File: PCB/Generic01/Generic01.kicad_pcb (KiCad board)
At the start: 2 copper layers, 13.2 x 18 mm, 3 parts, among them J1 Header, U1 ESP32-PICO-MINI-02

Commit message: Production files
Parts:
- moved Logo1 5.36 mm to (145.3, 118.1), turned to -90 degrees
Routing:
- net VCC: track 23.7 -> 21.7 mm
- net EN: track 14.8 -> 16.5 mm
- net RX: track 9.35 -> 9.96 mm
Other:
- board text added: "${CURRENT_DATE}"
- board text added: "3V3"
- board text added: "EN"
- board text added: "ESP32-01"
- board text added: "GND"
- board text added: "IO0"
- board text added: "IO2"
- board text added: "IO4"
- board text added: "RX"
- board text added: "TX"

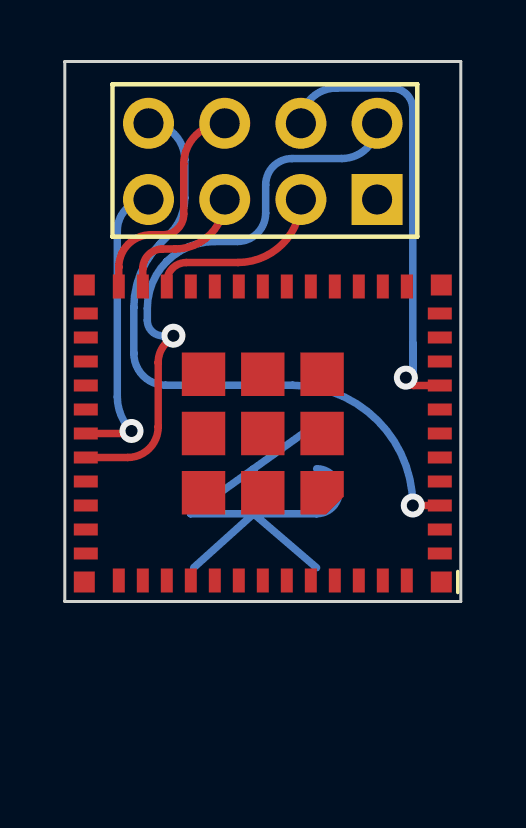
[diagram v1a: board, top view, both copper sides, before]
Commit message: Move RST
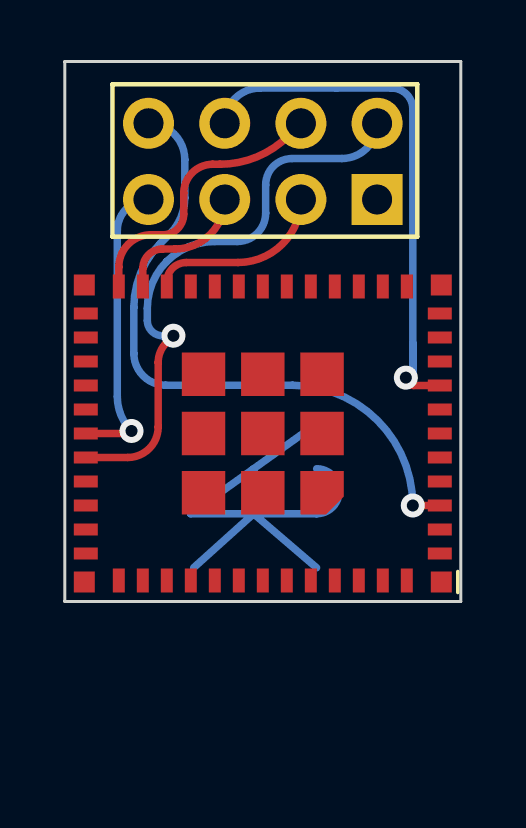
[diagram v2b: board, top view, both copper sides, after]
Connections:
- J1 pad 4: EN -> GPIO4
- J1 pad 6: GPIO4 -> EN
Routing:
- net EN: track 16.5 -> 19.1 mm
- net GPIO4: track 7.50 -> 9.27 mm
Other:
- board text added: "RST"
- board text removed: "EN"

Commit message: Tidy RST as EN
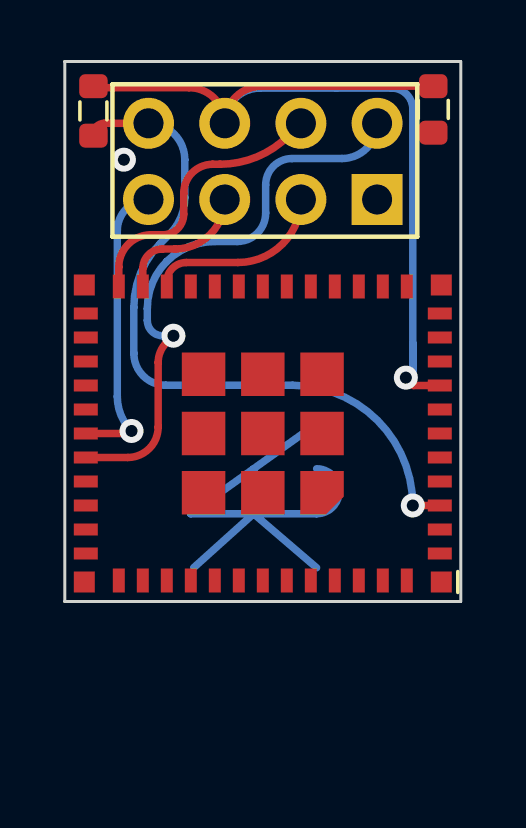
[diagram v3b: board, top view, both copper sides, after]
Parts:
- added C1: 1uF, RevK:C_0603, F.Cu at (151.3, 104.6)
- added R1: 12k, RevK:R_0603, F.Cu at (140.0, 104.6)
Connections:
- net EN renamed RST
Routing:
- net RST: track 19.1 -> 31.7 mm
- net VCC: track 21.7 -> 23.7 mm
- net GND: vias 0 -> 1
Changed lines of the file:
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@@
   (net 20 "unconnected-(U1-IO13-Pad20)")
   (net 21 "unconnected-(U1-IO15-Pad21)")
-  (net 22 "EN")
+  (net 22 "RST")
   (net 23 "unconnected-(U1-NC-Pad25)")
   (net 24 "unconnected-(U1-IO20-Pad26)")
@@
       (net 10 "unconnected-(U1-I39-Pad7)") (pinfunction "I39") (pintype "input+no_connect"))
     (pad "8" smd rect (at -5.9 1.6 180) (size 0.8 0.4) (layers "F.Cu" "F.Paste" "F.Mask")
-      (net 22 "EN") (pinfunction "EN") (pintype "input"))
+      (net 22 "RST") (pinfunction "EN") (pintype "input"))
     (pad "9" smd rect (at -5.9 2.4 180) (size 0.8 0.4) (layers "F.Cu" "F.Paste" "F.Mask")
       (net 11 "unconnected-(U1-I34-Pad9)") (pinfunction "I34") (pintype "input+no_connect"))
@@
     )
   )
+  (footprint "RevK:R_0603" (layer "F.Cu")
+    (at 139.954 104.648 90)
+    (descr "Capacitor SMD 0603 (1608 Metric), square (rectangular) end terminal, IPC_7351 nominal, (Body size source: IPC-SM-782 page 76, https://www.pcb-3d.com/wordpress/wp-content/uploads/ipc-sm-782a_amendment_1_and_2.pdf), generated with kicad-footprint-generator")
+    (tags "capacitor")
+    (property "Sheetfile" "Generic01.kicad_sch")
+    (property "Sheetname" "")
+    (property "ki_description" "Resistor")
+    (property "ki_keywords" "R res resistor")
+    (attr smd)
+    (fp_text reference "R1" (at -1.6 0 180) (layer "F.SilkS") hide
+        (effects (font (size 0.5 0.5) (thickness 0.08)))
+    )
+    (fp_text value "12k" (at 0 0 90) (layer "F.Fab")
+        (effects (font (size 0.4 0.4) (thickness 0.08)))
+    )
+    (fp_text user "${REFERENCE}" (at 0 -0.8 90) (layer "F.Fab")
+        (effects (font (size 0.4 0.4) (thickness 0.06)))
+    )
+    (fp_line (start -0.3 -0.45) (end 0.3 -0.45)
+      (stroke (width 0.12) (type solid)) (layer "F.SilkS"))
+    (fp_line (start -0.3 0.45) (end 0.3 0.45)
+      (stroke (width 0.12) (type solid)) (layer "F.SilkS"))
+    (fp_line (start -0.8 -0.4) (end 0.8 -0.4)
+      (stroke (width 0.05) (type solid)) (layer "F.CrtYd"))
+    (fp_line (start -0.8 0.4) (end -0.8 -0.4)
+      (stroke (width 0.05) (type solid)) (layer "F.CrtYd"))
+    (fp_line (start 0.8 -0.4) (end 0.8 0.4)
+      (stroke (width 0.05) (type solid)) (layer "F.CrtYd"))
+    (fp_line (start 0.8 0.4) (end -0.8 0.4)
+      (stroke (width 0.05) (type solid)) (layer "F.CrtYd"))
+    (fp_line (start -0.8 -0.4) (end 0.8 -0.4)
+      (stroke (width 0.1) (type solid)) (layer "F.Fab"))
+    (fp_line (start -0.8 0.4) (end -0.8 -0.4)
+      (stroke (width 0.1) (type solid)) (layer "F.Fab"))
+    (fp_line (start 0.8 -0.4) (end 0.8 0.4)
+      (stroke (width 0.1) (type solid)) (layer "F.Fab"))
+    (fp_line (start 0.8 0.4) (end -0.8 0.4)
+      (stroke (width 0.1) (type solid)) (layer "F.Fab"))
+    (pad "1" smd roundrect (at -0.825 0 90) (size 0.8 0.95) (layers "F.Cu" "F.Paste" "F.Mask") (roundrect_rratio 0.25)
+      (net 6 "VCC") (pintype "passive"))
+    (pad "2" smd roundrect (at 0.825 0 90) (size 0.8 0.95) (layers "F.Cu" "F.Paste" "F.Mask") (roundrect_rratio 0.25)
+      (net 22 "RST") (pintype "passive"))
+    (model "${KICAD6_3DMODEL_DIR}/Resistor_SMD.3dshapes/R_0603_1608Metric.step"
+      (offset (xyz 0 0 0))
+      (scale (xyz 1 1 1))
+      (rotate (xyz 0 0 0))
+    )
+  )
+  (footprint "RevK:C_0603" (layer "F.Cu")
+    (at 151.2824 104.5972 -90)
+    (descr "Capacitor SMD 0603 (1608 Metric), square (rectangular) end terminal, IPC_7351 nominal, (Body size source: IPC-SM-782 page 76, https://www.pcb-3d.com/wordpress/wp-content/uploads/ipc-sm-782a_amendment_1_and_2.pdf), generated with kicad-footprint-generator")
+    (tags "capacitor")
+    (property "Sheetfile" "Generic01.kicad_sch")
+    (property "Sheetname" "")
+    (property "ki_description" "Unpolarized capacitor")
+    (property "ki_keywords" "cap capacitor")
+    (attr smd)
+    (fp_text reference "C1" (at -1.6 0) (layer "F.SilkS") hide
+        (effects (font (size 0.5 0.5) (thickness 0.08)))
+    )
+    (fp_text value "1uF" (at 0 0 90) (layer "F.Fab")
+        (effects (font (size 0.4 0.4) (thickness 0.08)))
+    )
+    (fp_text user "${REFERENCE}" (at 0 -0.8 90) (layer "F.Fab")
+        (effects (font (size 0.4 0.4) (thickness 0.06)))
+    )
+    (fp_line (start -0.3 -0.5) (end 0.3 -0.5)
+      (stroke (width 0.12) (type solid)) (layer "F.SilkS"))
+    (fp_line (start -0.3 0.5) (end 0.3 0.5)
+      (stroke (width 0.12) (type solid)) (layer "F.SilkS"))
+    (fp_line (start -0.8 -0.4) (end 0.8 -0.4)
+      (stroke (width 0.05) (type solid)) (layer "F.CrtYd"))
+    (fp_line (start -0.8 0.4) (end -0.8 -0.4)
+      (stroke (width 0.05) (type solid)) (layer "F.CrtYd"))
+    (fp_line (start 0.8 -0.4) (end 0.8 0.4)
+      (stroke (width 0.05) (type solid)) (layer "F.CrtYd"))
+    (fp_line (start 0.8 0.4) (end -0.8 0.4)
+      (stroke (width 0.05) (type solid)) (layer "F.CrtYd"))
+    (fp_line (start -0.8 -0.4) (end 0.8 -0.4)
+      (stroke (width 0.1) (type solid)) (layer "F.Fab"))
+    (fp_line (start -0.8 0.4) (end -0.8 -0.4)
+      (stroke (width 0.1) (type solid)) (layer "F.Fab"))
+    (fp_line (start 0.8 -0.4) (end 0.8 0.4)
+      (stroke (width 0.1) (type solid)) (layer "F.Fab"))
+    (fp_line (start 0.8 0.4) (end -0.8 0.4)
+      (stroke (width 0.1) (type solid)) (layer "F.Fab"))
+    (pad "1" smd roundrect (at -0.775 0 270) (size 0.8 0.95) (layers "F.Cu" "F.Paste" "F.Mask") (roundrect_rratio 0.25)
+      (net 22 "RST") (pintype "passive"))
+    (pad "2" smd roundrect (at 0.775 0 270) (size 0.8 0.95) (layers "F.Cu" "F.Paste" "F.Mask") (roundrect_rratio 0.25)
+      (net 2 "GND") (pintype "passive"))
+    (model "${KICAD6_3DMODEL_DIR}/Capacitor_SMD.3dshapes/C_0603_1608Metric.step"
+      (offset (xyz 0 0 0))
+      (scale (xyz 1 1 1))
+      (rotate (xyz 0 0 0))
+    )
+  )
   (footprint "Connector_PinHeader_2.54mm:PinHeader_2x04_P2.54mm_Vertical" (layer "B.Cu")
     (at 149.41 107.6 90)
@@
       (net 28 "GPIO0") (pinfunction "Pin_5") (pintype "passive"))
     (pad "6" thru_hole oval (at 2.54 -5.08 90) (size 1.7 1.7) (drill 1) (layers "*.Cu" "*.Mask")
-      (net 22 "EN") (pinfunction "Pin_6") (pintype "passive"))
+      (net 22 "RST") (pinfunction "Pin_6") (pintype "passive"))
     (pad "7" thru_hole oval (at 0 -7.62 90) (size 1.7 1.7) (drill 1) (layers "*.Cu" "*.Mask")
       (net 5 "RX") (pinfunction "Pin_7") (pintype "passive"))
@@
   (arc (start 149.41 105.06) (mid 149.065994 105.890505) (end 148.235489 106.234511) (width 0.25) (layer "B.Cu") (net 1))
   (arc (start 144 109) (mid 143.133935 109.172271) (end 142.39972 109.662857) (width 0.25) (layer "B.Cu") (net 1))
+  (via (at 140.97 106.2736) (size 0.8) (drill 0.4) (layers "F.Cu" "B.Cu") (free) (net 2))
   (segment (start 143.049711 109.700289) (end 144.769711 109.700289) (width 0.25) (layer "F.Cu") (net 3))
   (arc (start 142.4 110.35) (mid 142.590296 109.890585) (end 143.049711 109.700289) (width 0.25) (layer "F.Cu") (net 3))
@@
   (arc (start 141.224 115.316) (mid 140.873189 114.790974) (end 140.75 114.171663) (width 0.25) (layer "B.Cu") (net 5))
   (arc (start 140.75 108.64) (mid 141.054609 107.904609) (end 141.79 107.6) (width 0.25) (layer "B.Cu") (net 5))
+  (segment (start 141.79 105.06) (end 140.317 105.06) (width 0.25) (layer "F.Cu") (net 6))
   (segment (start 151.5 117.8) (end 150.6 117.8) (width 0.25) (layer "F.Cu") (net 6))
   (via (at 150.6 117.8) (size 0.8) (drill 0.4) (layers "F.Cu" "B.Cu") (net 6))
+  (arc (start 140.317 105.06) (mid 140.06032 105.16632) (end 139.954 105.423) (width 0.25) (layer "F.Cu") (net 6))
   (segment (start 142.5 108.75) (end 142.184372 109.065627) (width 0.25) (layer "B.Cu") (net 6))
   (segment (start 142.367 113.792) (end 146.592 113.792) (width 0.25) (layer "B.Cu") (net 6))
@@
   (arc (start 141.79 105.06) (mid 142.645599 105.414401) (end 143 106.27) (width 0.25) (layer "B.Cu") (net 6))
   (segment (start 150.63 113.8) (end 151.5 113.8) (width 0.25) (layer "F.Cu") (net 22))
+  (segment (start 151.2824 103.8222) (end 145.5678 103.8222) (width 0.25) (layer "F.Cu") (net 22))
+  (segment (start 139.954 103.873) (end 143.143 103.873) (width 0.25) (layer "F.Cu") (net 22))
   (via (at 150.368 113.538) (size 0.8) (drill 0.4) (layers "F.Cu" "B.Cu") (net 22))
+  (arc (start 143.143 103.873) (mid 143.982336 104.220664) (end 144.33 105.06) (width 0.25) (layer "F.Cu") (net 22))
   (arc (start 150.63 113.8) (mid 150.444738 113.723262) (end 150.368 113.538) (width 0.25) (layer "F.Cu") (net 22))
+  (arc (start 145.5678 103.8222) (mid 144.692543 104.184743) (end 144.33 105.06) (width 0.25) (layer "F.Cu") (net 22))
   (segment (start 148.044022 103.885) (end 145.505 103.885) (width 0.25) (layer "B.Cu") (net 22))
   (segment (start 150.6 113.306) (end 150.6 112.395) (width 0.25) (layer "B.Cu") (net 22))
